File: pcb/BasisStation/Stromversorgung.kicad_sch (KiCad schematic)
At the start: 13 parts

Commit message: v0.00.001 fix(SHBS-4): +3V3 global verbunden, Symbolbibliothek entkoppelt
Die Projektbibliothek war in sym-lib-table unter dem Nickname "power"
registriert und verdeckte damit die gleichnamige KiCad-Standardbibliothek.
power:GND (28x), power:PWR_FLAG und power:+3V3 waren dadurch projektweit
nicht aufloesbar. Nickname auf "shbs_power" geaendert, lib_id von PS1 und
J_PWR1 samt ihrer lib_symbols-Cache-Eintraege nachgezogen. Alle uebrigen
power:*-Referenzen bleiben unveraendert und loesen jetzt gegen die
KiCad-Standardbibliothek auf.

Darauf aufbauend: +3V3 lag auf beiden Blaettern als lokales Label vor und
war damit blattlokal - der Buck-Ausgang erreichte U6 nicht (ERC
power_pin_not_driven an U6 Pin 2). Alle drei Vorkommen durch platzierte
power:+3V3-Symbole ersetzt (#PWR100 bis #PWR102).

Beide Schritte in einem Commit, weil power:+3V3 erst nach der Umbenennung
aufloesbar ist und die Aenderungen dieselbe Dateistelle betreffen.

ERC: 53 -> 29 Meldungen.

Co-Authored-By: Claude Opus 5 <noreply@anthropic.com>
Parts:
- J_PWR1: symbol power:USB_C_Receptacle_Power -> shbs_power:USB_C_Receptacle_Power
- PS1: symbol power:MP2359DJ -> shbs_power:MP2359DJ
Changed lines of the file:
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@@
 		)
 	)
-	(label "+3V3"
-		(at 185.42 138.43 0)
+	(symbol
+		(lib_id "power:+3V3")
+		(at 190.5 138.43 0)
+		(unit 1)
+		(exclude_from_sim no)
+		(in_bom yes)
+		(on_board yes)
+		(dnp no)
+		(fields_autoplaced yes)
+		(property "Reference" "#PWR100"
+			(at 190.5 132.08 0)
+			(effects
+				(font
+					(size 1.27 1.27)
+				)
+				(hide yes)
+			)
+		)
+		(property "Value" "+3V3"
+			(at 190.5 134.874 0)
+			(effects
+				(font
+					(size 1.27 1.27)
+				)
+			)
+		)
+		(property "Footprint" ""
+			(at 190.5 138.43 0)
+			(effects
+				(font
+					(size 1.27 1.27)
+				)
+				(hide yes)
+			)
+		)
+		(property "Datasheet" ""
+			(at 190.5 138.43 0)
+			(effects
+				(font
+					(size 1.27 1.27)
+				)
+				(hide yes)
+			)
+		)
+		(property "Description" "Power symbol creates a global label with name \"+3V3\""
+			(at 190.5 138.43 0)
+			(effects
+				(font
+					(size 1.27 1.27)
+				)
+				(hide yes)
+			)
+		)
+		(pin "1"
+		)
+		(instances
+			(project "BasisStation"
+				(path "/498c7092-55c1-4229-9f4b-13c6a8e7da47/5fd3b213-b7bb-4f0b-b520-d744bf60efa7"
+					(reference "#PWR100")
+					(unit 1)
+				)
+			)
+		)
+	)
+	(global_label "PW_EN"
+		(shape input)
+		(at 161.29 77.47 90)
+		(fields_autoplaced yes)
 		(effects
 			(font
 				(size 1.27 1.27)
 			)
-			(justify left bottom)
+			(justify left)
+		)
+		(property "Intersheetrefs" "${INTERSHEET_REFS}"
+			(at 161.29 68.3163 90)
+			(effects
+				(font
+					(size 1.27 1.27)
+				)
+				(justify left)
+				(hide yes)
+			)
 		)
 	)
 	(global_label "PW_EN"
-		(shape input)
-		(at 161.29 77.47 90)
+		(shape output)
+		(at 137.16 93.98 270)
 		(fields_autoplaced yes)
 		(effects
@@
 				(size 1.27 1.27)
 			)
-			(justify left)
-		)
-		(property "Intersheetrefs" "${INTERSHEET_REFS}"
-			(at 161.29 68.3163 90)
-			(effects
-				(font
-					(size 1.27 1.27)
-				)
-				(justify left)
-				(hide yes)
-			)
-		)
-	)
-	(global_label "PW_EN"
-		(shape output)
-		(at 137.16 93.98 270)
-		(fields_autoplaced yes)
-		(effects
-			(font
-				(size 1.27 1.27)
-			)
 			(justify right)
 		)
@@
 	)
 	(symbol
-		(lib_id "power:USB_C_Receptacle_Power")
+		(lib_id "shbs_power:USB_C_Receptacle_Power")
 		(at 246.38 83.82 0)
 		(unit 1)
@@
 	)
 	(symbol
-		(lib_id "power:MP2359DJ")
+		(lib_id "shbs_power:MP2359DJ")
 		(at 148.59 86.36 0)
 		(unit 1)

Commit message: v0.00.001 chore(SHBS-4): Symbole aus Bibliothek aktualisiert
KiCad-Lauf "Symbole aus Bibliothek aktualisieren" (Bediener): die zuvor per
Text-Edit erzeugte power:+3V3-Cache-Definition wurde durch das
Bibliotheksoriginal ersetzt (abweichende Referenz-Position, Pfeil aus zwei
Polylines), lib_symbols alphabetisch sortiert.

Laut report.txt aktualisieren #PWR100-#PWR102 (power:+3V3), PS1
(shbs_power:MP2359DJ) und J_PWR1 (shbs_power:USB_C_Receptacle_Power)
fehlerfrei - die Bibliotheksentkopplung aus da60c97 traegt.

ERC: 29 -> 14 Meldungen (4 Fehler, 10 Warnungen). Die verbleibenden Fehler
sind ausschliesslich power_pin_not_driven an U6.2, PS1.5, J_PWR1.A4 und
#PWR100 und haengen an PWR_FLAG/Buck-Topologie (SHBS-4 offen).

Co-Authored-By: Claude Opus 5 <noreply@anthropic.com>
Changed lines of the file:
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@@
-		)
-	)
-	(symbol
-		(lib_id "power:+3V3")
-		(at 190.5 138.43 0)
-		(unit 1)
-		(exclude_from_sim no)
-		(in_bom yes)
-		(on_board yes)
-		(dnp no)
-		(fields_autoplaced yes)
-		(property "Reference" "#PWR100"
-			(at 190.5 132.08 0)
-			(effects
-				(font
-					(size 1.27 1.27)
-				)
-				(hide yes)
-			)
-		)
-		(property "Value" "+3V3"
-			(at 190.5 134.874 0)
-			(effects
-				(font
-					(size 1.27 1.27)
-				)
-			)
-		)
-		(property "Footprint" ""
-			(at 190.5 138.43 0)
-			(effects
-				(font
-					(size 1.27 1.27)
-				)
-				(hide yes)
-			)
-		)
-		(property "Datasheet" ""
-			(at 190.5 138.43 0)
-			(effects
-				(font
-					(size 1.27 1.27)
-				)
-				(hide yes)
-			)
-		)
-		(property "Description" "Power symbol creates a global label with name \"+3V3\""
-			(at 190.5 138.43 0)
-			(effects
-				(font
-					(size 1.27 1.27)
-				)
-				(hide yes)
-			)
-		)
-		(pin "1"
-		)
-		(instances
-			(project "BasisStation"
-				(path "/498c7092-55c1-4229-9f4b-13c6a8e7da47/5fd3b213-b7bb-4f0b-b520-d744bf60efa7"
-					(reference "#PWR100")
-					(unit 1)
-				)
-			)
 		)
 	)
@@
 					(unit 1)
 				)
+			)
+		)
+	)
+	(symbol
+		(lib_id "power:+3V3")
+		(at 190.5 138.43 0)
+		(unit 1)
+		(exclude_from_sim no)
+		(in_bom yes)
+		(on_board yes)
+		(dnp no)
+		(fields_autoplaced yes)
+		(property "Reference" "#PWR100"
+			(at 190.5 132.08 0)
+			(effects
+				(font
+					(size 1.27 1.27)
+				)
+				(hide yes)
+			)
+		)
+		(property "Value" "+3V3"
+			(at 190.5 134.874 0)
+			(effects
+				(font
+					(size 1.27 1.27)
+				)
+			)
+		)
+		(property "Footprint" ""
+			(at 190.5 138.43 0)
+			(effects
+				(font
+					(size 1.27 1.27)
+				)
+				(hide yes)
+			)
+		)
+		(property "Datasheet" ""
+			(at 190.5 138.43 0)
+			(effects
+				(font
+					(size 1.27 1.27)
+				)
+				(hide yes)
+			)
+		)
+		(property "Description" "Power symbol creates a global label with name \"+3V3\""
+			(at 190.5 138.43 0)
+			(effects
+				(font
+					(size 1.27 1.27)
+				)
+				(hide yes)
+			)
+		)
+		(pin "1"
+		)
+		(instances
+			(project "BasisStation"
+				(path "/498c7092-55c1-4229-9f4b-13c6a8e7da47/5fd3b213-b7bb-4f0b-b520-d744bf60efa7"
+					(reference "#PWR100")
+					(unit 1)
+				)

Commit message: v0.00.001 fix(SHBS-4): PWR_FLAG an VBUS, VIN und Buck-Ausgang ergaenzt
Das Projekt enthielt keine einzige platzierte PWR_FLAG - die bisherige
Annahme "4x im Layout" zaehlte Treffer in der lib_symbols-Definition,
nicht Instanzen. Dadurch meldete die ERC power_pin_not_driven an
J_PWR1.A4 [VBUS] und PS1.5 [VIN].

Drei Flags noetig statt zwei: F1 und L1 sind passiv und propagieren keine
Power-Quelle, der 3,3-V-Rail hat gar keinen Power-Output-Pin.

  #FLG01  VBUS vor F1      Stich ab (226,06 / 78,74)
  #FLG02  VIN hinter F1    Stich ab (190,5 / 83,82)
  #FLG03  Buck-Ausgang     Stich ab (181,61 / 138,43)

Per ERC-Lauf 2026-09-15 21:39 bestaetigt: Fehler 4 -> 2, die beiden
Eingangsfehler entfallen.

Co-Authored-By: Claude Opus 5 <noreply@anthropic.com>
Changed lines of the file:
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@@
+		)
+	)
+	(junction
+		(at 226.06 78.74)
+		(diameter 0)
+		(color 0 0 0 0)
+	)
+	(junction
+		(at 190.5 83.82)
+		(diameter 0)
+		(color 0 0 0 0)
+	)
+	(junction
+		(at 181.61 138.43)
+		(diameter 0)
+		(color 0 0 0 0)
+	)
+	(wire
+		(pts
+			(xy 226.06 78.74) (xy 226.06 73.66)
+		)
+		(stroke
+			(width 0)
+			(type default)
+		)
+	)
+	(wire
+		(pts
+			(xy 190.5 83.82) (xy 190.5 78.74)
+		)
+		(stroke
+			(width 0)
+			(type default)
+		)
+	)
+	(wire
+		(pts
+			(xy 181.61 138.43) (xy 181.61 143.51)
+		)
+		(stroke
+			(width 0)
+			(type default)
+		)
+	)
+	(symbol
+		(lib_id "power:PWR_FLAG")
+		(at 226.06 73.66 0)
+		(unit 1)
+		(exclude_from_sim no)
+		(in_bom yes)
+		(on_board yes)
+		(dnp no)
+		(fields_autoplaced yes)
+		(property "Reference" "#FLG01"
+			(at 226.06 71.755 0)
+			(effects
+				(font
+					(size 1.27 1.27)
+				)
+				(hide yes)
+			)
+		)
+		(property "Value" "PWR_FLAG"
+			(at 226.06 69.85 0)
+			(effects
+				(font
+					(size 1.27 1.27)
+				)
+			)
+		)
+		(property "Footprint" ""
+			(at 226.06 73.66 0)
+			(effects
+				(font
+					(size 1.27 1.27)
+				)
+				(hide yes)
+			)
+		)
+		(property "Datasheet" "~"
+			(at 226.06 73.66 0)
+			(effects
+				(font
+					(size 1.27 1.27)
+				)
+				(hide yes)
+			)
+		)
+		(property "Description" "Special symbol for telling ERC where power comes from"
+			(at 226.06 73.66 0)
+			(effects
+				(font
+					(size 1.27 1.27)
+				)
+				(hide yes)
+			)
+		)
+		(pin "1"
+		)
+		(instances
+			(project "BasisStation"
+				(path "/498c7092-55c1-4229-9f4b-13c6a8e7da47/5fd3b213-b7bb-4f0b-b520-d744bf60efa7"
+					(reference "#FLG01")
+					(unit 1)
+				)
+			)
+		)
+	)
+	(symbol
+		(lib_id "power:PWR_FLAG")
+		(at 190.5 78.74 0)
+		(unit 1)
+		(exclude_from_sim no)
+		(in_bom yes)
+		(on_board yes)
+		(dnp no)
+		(fields_autoplaced yes)
+		(property "Reference" "#FLG02"
+			(at 190.5 76.835 0)
+			(effects
+				(font
+					(size 1.27 1.27)
+				)
+				(hide yes)
+			)
+		)
+		(property "Value" "PWR_FLAG"
+			(at 190.5 74.93 0)
+			(effects
+				(font
+					(size 1.27 1.27)
+				)
+			)
+		)
+		(property "Footprint" ""
+			(at 190.5 78.74 0)
+			(effects
+				(font
+					(size 1.27 1.27)
+				)
+				(hide yes)
+			)
+		)
+		(property "Datasheet" "~"
+			(at 190.5 78.74 0)
+			(effects
+				(font
+					(size 1.27 1.27)
+				)
+				(hide yes)
+			)
+		)
+		(property "Description" "Special symbol for telling ERC where power comes from"
+			(at 190.5 78.74 0)
+			(effects
+				(font
+					(size 1.27 1.27)
+				)
+				(hide yes)
+			)
+		)
+		(pin "1"
+		)
+		(instances
+			(project "BasisStation"
+				(path "/498c7092-55c1-4229-9f4b-13c6a8e7da47/5fd3b213-b7bb-4f0b-b520-d744bf60efa7"
+					(reference "#FLG02")
+					(unit 1)
+				)
+			)
+		)
+	)
+	(symbol
+		(lib_id "power:PWR_FLAG")
+		(at 181.61 143.51 180)
+		(unit 1)
+		(exclude_from_sim no)
+		(in_bom yes)
+		(on_board yes)
+		(dnp no)
+		(fields_autoplaced yes)
+		(property "Reference" "#FLG03"
+			(at 181.61 145.415 0)
+			(effects
+				(font
+					(size 1.27 1.27)
+				)
+				(hide yes)
+			)
+		)
+		(property "Value" "PWR_FLAG"
+			(at 181.61 147.32 0)
+			(effects
+				(font
+					(size 1.27 1.27)
+				)
+			)
+		)
+		(property "Footprint" ""
+			(at 181.61 143.51 0)
+			(effects
+				(font
+					(size 1.27 1.27)
+				)
+				(hide yes)
+			)
+		)
+		(property "Datasheet" "~"
+			(at 181.61 143.51 0)
+			(effects
+				(font
+					(size 1.27 1.27)
+				)
+				(hide yes)
+			)
+		)
+		(property "Description" "Special symbol for telling ERC where power comes from"
+			(at 181.61 143.51 0)
+			(effects
+				(font
+					(size 1.27 1.27)
+				)
+				(hide yes)
+			)
+		)
+		(pin "1"
+		)
+		(instances
+			(project "BasisStation"
+				(path "/498c7092-55c1-4229-9f4b-13c6a8e7da47/5fd3b213-b7bb-4f0b-b520-d744bf60efa7"
+					(reference "#FLG03")
+					(unit 1)
+				)
+			)
 		)
 	)

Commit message: v0.00.001 fix(SHBS-4): Footprints fuer F1 und R17-R20 zugewiesen
Pruefung ueber alle Blaetter ergab acht Bauteile ohne Footprint-Feld.
Ohne Zuweisung uebernimmt der PCB-Abgleich (F8) sie nicht, was den
anstehenden Netzlisten-Export blockiert haette.

  F1        Fuse:Fuse_1206_3216Metric
  R17-R20   Resistor_SMD:R_0805_2012Metric

Werte gemaess Stueckliste in docs/project/power_supply.md. J1 bleibt
offen bis SHBS-6 (Umstellung auf USB-C), ANT1 und ANT2 sind BOM-only
und bewusst ohne Footprint.

Co-Authored-By: Claude Opus 5 <noreply@anthropic.com>
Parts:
- F1: footprint (none) -> Fuse:Fuse_1206_3216Metric
- R17, R18, R19, R20: footprint (none) -> Resistor_SMD:R_0805_2012Metric
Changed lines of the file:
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@@
 			)
 		)
-		(property "Footprint" ""
+		(property "Footprint" "Resistor_SMD:R_0805_2012Metric"
 			(at 229.362 95.25 90)
 			(effects
@@
 			)
 		)
-		(property "Footprint" ""
+		(property "Footprint" "Fuse:Fuse_1206_3216Metric"
 			(at 203.2 82.042 90)
 			(effects
@@
 			)
 		)
-		(property "Footprint" ""
+		(property "Footprint" "Resistor_SMD:R_0805_2012Metric"
 			(at 113.538 97.79 90)
 			(effects
@@
 			)
 		)
-		(property "Footprint" ""
+		(property "Footprint" "Resistor_SMD:R_0805_2012Metric"
 			(at 126.238 97.79 90)
 			(effects
@@
 			)
 		)
-		(property "Footprint" ""
+		(property "Footprint" "Resistor_SMD:R_0805_2012Metric"
 			(at 217.932 95.25 90)
 			(effects

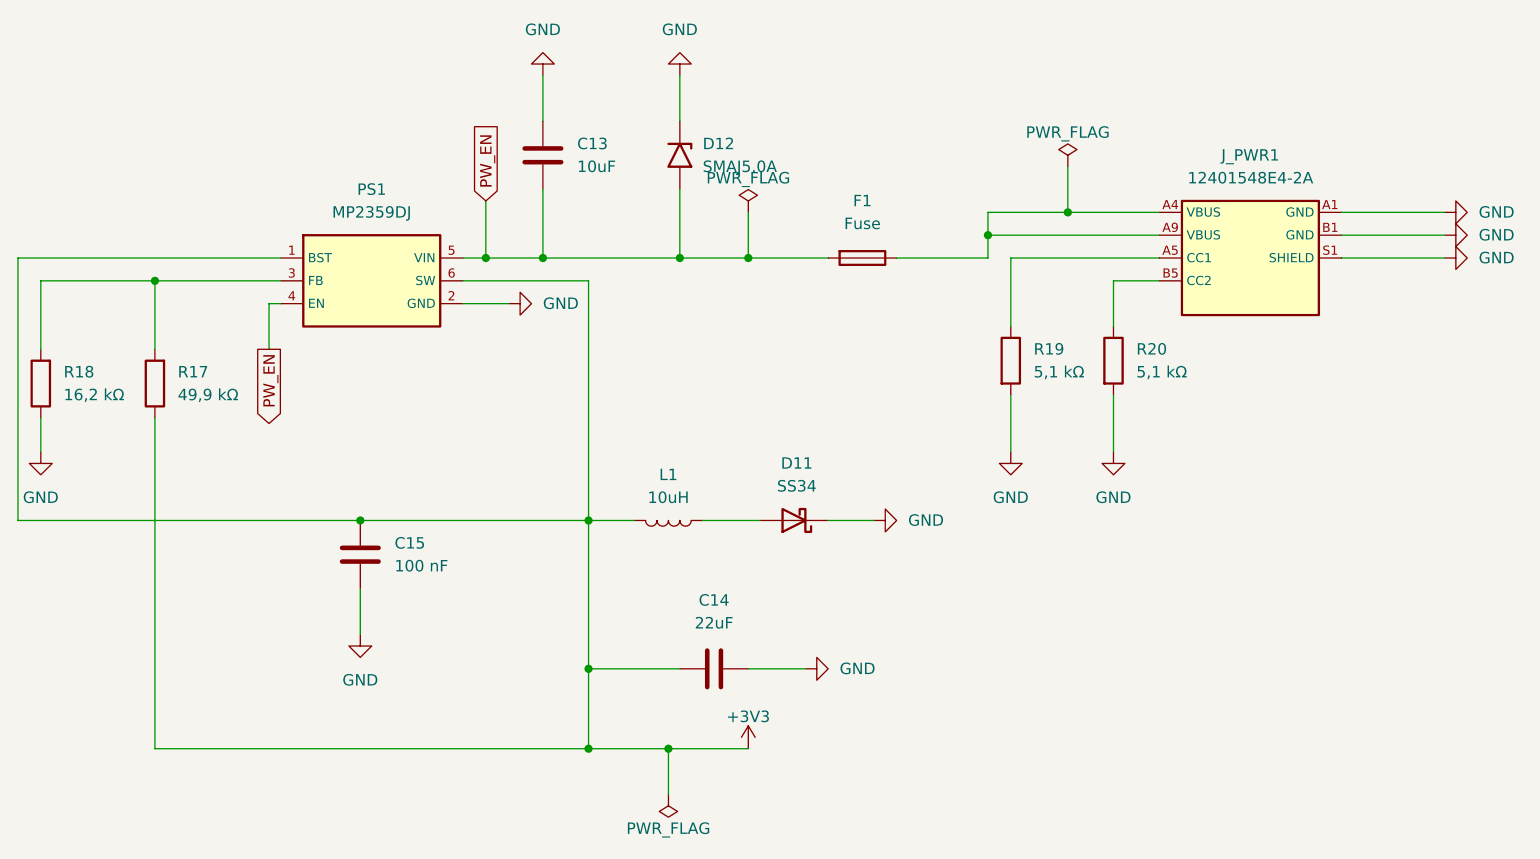
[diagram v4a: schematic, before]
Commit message: v0.00.001 fix(SHBS-4): Buck-Ausgangszweig korrigiert, ERC fehlerfrei
Der Ausgangszweig des MP2359 war so verdrahtet, dass das Netz mit dem
+3V3-Label elektrisch der Schaltknoten SW war. D11 lag verpolt hinter L1
(Anode am Ausgang, Kathode an GND) und haette den Ausgang kurzgeschlossen,
C15 lag gegen GND statt als Bootstrap zwischen BST und SW, wodurch der
MP2359 sein High-Side-Gate nicht haette treiben koennen, und C14/R17
hingen am Schaltknoten statt am geglaetteten Ausgang.

Korrektur vom Bediener in der KiCad-GUI ausgefuehrt, Vorlage siehe
tmp/report/2026-09-15_shbs-4-buck-ausgangszweig.md. Netzpruefung aus der
Schaltplandatei:

  SW     PS1.6, C15.2, D11.1 (K), L1.2
  BST    PS1.1, C15.1
  +3V3   L1.1, C14.2, R17.1, #PWR100, #FLG03
  GND    D11.2 (A), C14.1, R18.1, PS1.2
  FB     PS1.3, R17.2, R18.2

Kein unverbundener Pin im Power-Zweig. ERC-Lauf 2026-09-15 22:27:
0 Fehler, 9 unkritische Warnungen (Metadaten-Mismatch von SnapEDA-Symbolen,
Drahtstummel am EN-Netz, S2/J1, GND/EPAD) - alle ausserhalb der Power-Kette.

BasisStation.net neu exportiert: keine PS2- und +12V-Reste mehr, und +3V3
fuehrt jetzt L1.1 und U6.2 im selben Netz. An den uebrigen Blaettern hat
KiCad nur Zeilenenden normalisiert bzw. die Float-Darstellung von #PWR103
gerundet.

Co-Authored-By: Claude Opus 5 <noreply@anthropic.com>
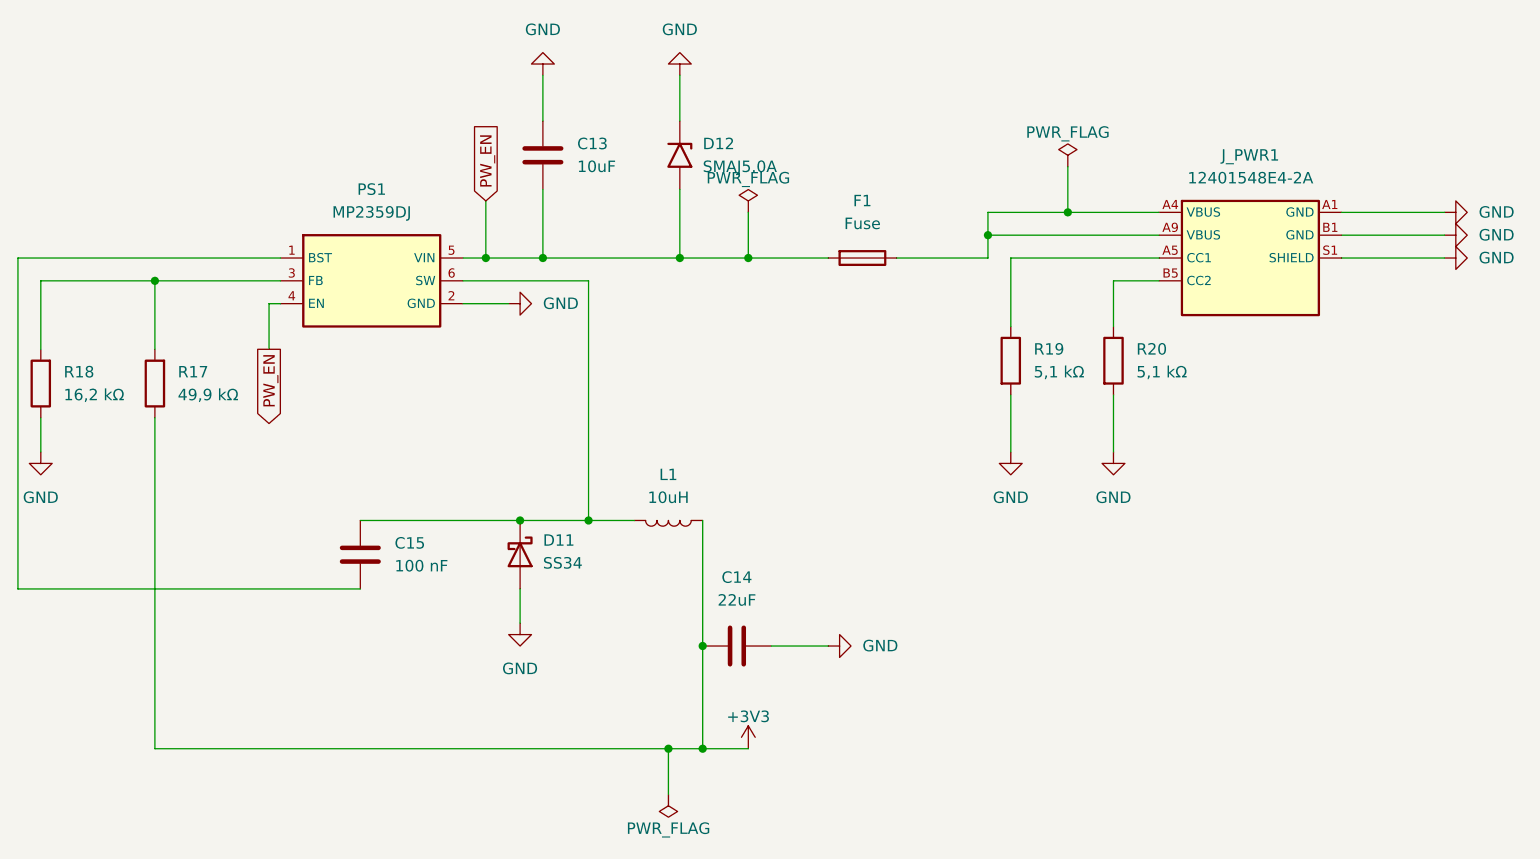
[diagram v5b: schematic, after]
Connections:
- net +3V3: now also L1.1; no longer C15.2, L1.2, PS1.1 (BST), PS1.6 (SW)
- net GND: now also D11.2 (A); no longer C15.1, D11.1 (K)
- new net: C15.2, D11.1 (K), L1.2, PS1.6 (SW)
- new net: C15.1, PS1.1 (BST)
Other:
- moved on the sheet: C14, D11
